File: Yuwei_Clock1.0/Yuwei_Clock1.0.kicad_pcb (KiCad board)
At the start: 2 copper layers, 140 x 90 mm, 4 parts

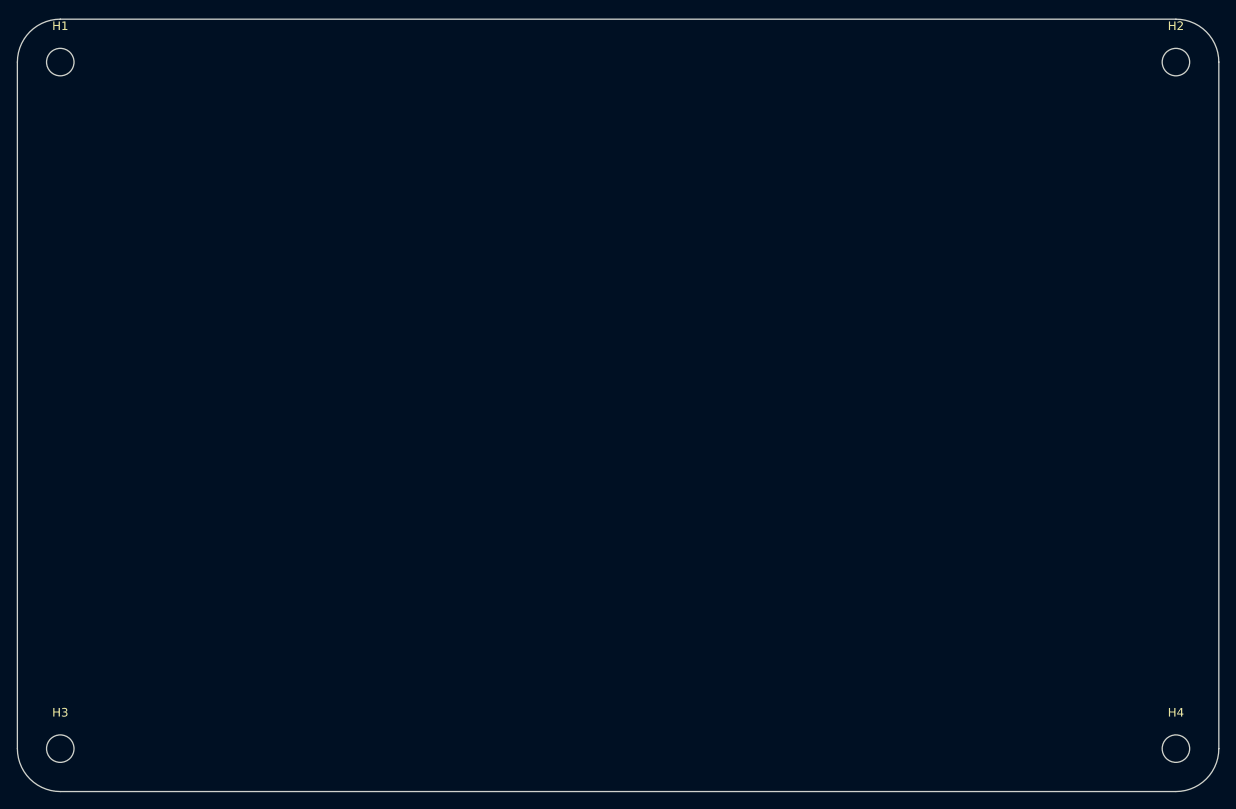
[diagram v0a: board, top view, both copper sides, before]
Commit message: Change polar capacitor to C_0805_10uf
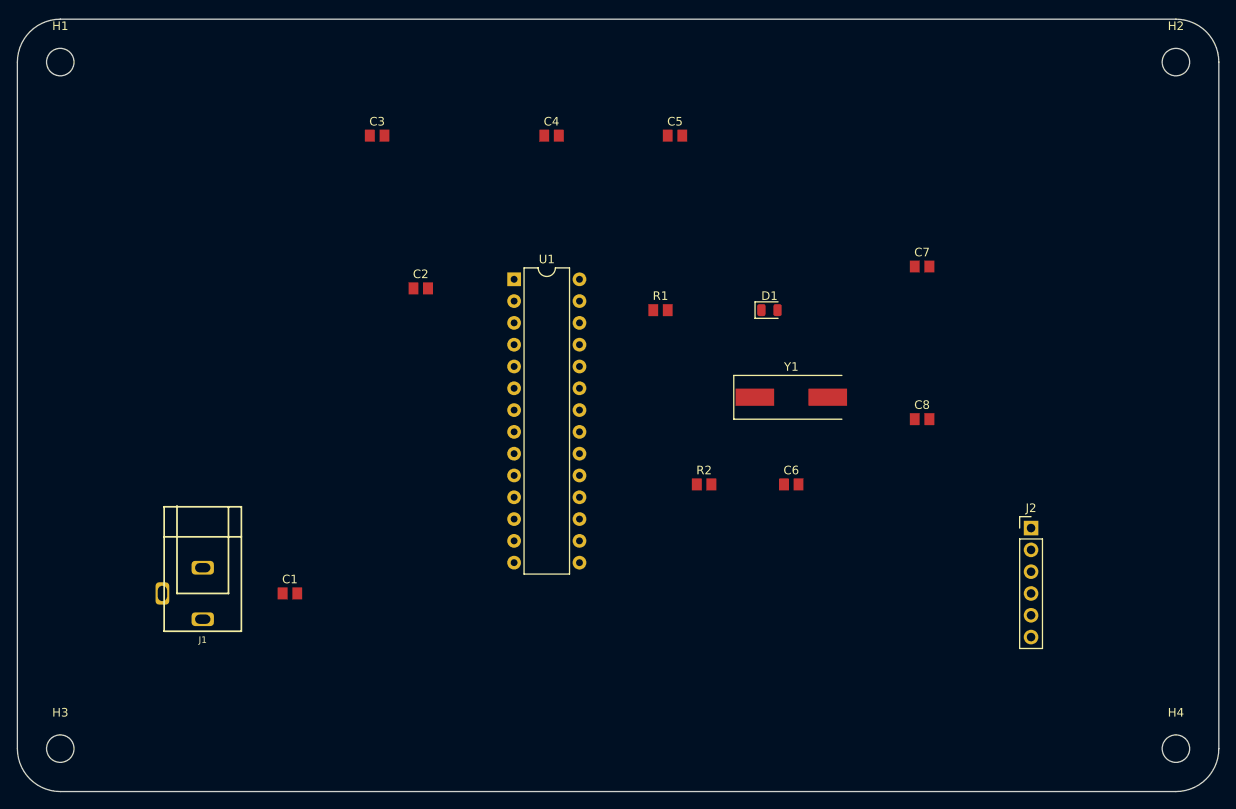
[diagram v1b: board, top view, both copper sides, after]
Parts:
- added C1: C_0805_10uf, footprints:C_0805_2012Metric, F.Cu at (111.8, 121.9)
- added C2: C_0805_10uf, footprints:C_0805_2012Metric, F.Cu at (127.0, 86.4)
- added C3: C_0805_10uf, footprints:C_0805_2012Metric, F.Cu at (121.9, 68.6)
- added C4: C_0805_10uf, footprints:C_0805_2012Metric, F.Cu at (142.2, 68.6)
- added C5: C_0805_10uf, footprints:C_0805_2012Metric, F.Cu at (156.6, 68.6)
- added C6: C_0805_0.1uf, footprints:C_0805_2012Metric, F.Cu at (170.2, 109.2)
- added C7: C_0805_22pf, footprints:C_0805_2012Metric, F.Cu at (185.4, 83.8)
- added C8: C_0805_22pf, footprints:C_0805_2012Metric, F.Cu at (185.4, 101.6)
- added D1: LED_0805, footprints:LED_0805_2012Metric, F.Cu at (167.6, 88.9)
- added J1: PJ-102AH, footprints:PJ-102AH, F.Cu at (101.6, 121.9)
- added J2: Conn_01x06, footprints:PinHeader_1x06_P2.54mm_Vertical, F.Cu at (198.1, 114.3)
- added R1: R_0805_2.2K, footprints:R_0805_2012Metric, F.Cu at (154.9, 88.9)
- added R2: R_0805_10K, footprints:R_0805_2012Metric, F.Cu at (160.0, 109.2)
- added U1: ATmega328-PU, footprints:DIP-28_W7.62mm, F.Cu at (137.9, 85.3)
- added Y1: Crystal_16MHz, footprints:Crystal_SMD_HC49-SD, F.Cu at (170.2, 99.1)

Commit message: Update with Schematic and PCB
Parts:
- removed C8: C_0805_22pf, footprints:C_0805_2012Metric
- removed J1: PJ-102AH, footprints:PJ-102AH
- added J?: Conn_01x06, footprints:PinHeader_1x06_P2.54mm_Vertical, F.Cu at (152.0, 82.1)
- added R3: R_0805_47, footprints:R_0805_2012Metric, F.Cu at (156.5, 97.1)
- added R4: R_0805_47, footprints:R_0805_2012Metric, F.Cu at (172.1, 81.3)
- added SW1: Omron_B3F_SPST, footprints:SW_SPST_Omron_B3FS-100xP, F.Cu at (143.8, 112.0)
- added U2: L7805, footprints:TO-220-3_Horizontal_TabDown, F.Cu at (141.4, 100.0)
- C2, C3: value C_0805_10uf -> C_0805_0.1uf
- C4, C5: value C_0805_10uf -> C_0805_22pf
- C6: value C_0805_0.1uf -> C_0805_1uf
- C7: value C_0805_22pf -> C_0805_1uf
- J2: value Conn_01x06 -> PJ-102AH; footprint footprints:PinHeader_1x06_P2.54mm_Vertical -> footprints:PJ-102AH
- moved C1 69.1 mm to (167.6, 81.3)
- moved C5 57.6 mm to (133.9, 121.5)
- moved C3 48.3 mm to (167.6, 84.2)
- moved D1 48.2 mm to (129.5, 118.5)
- moved J2 44.6 mm to (160.3, 90.6)
- moved R1 41.3 mm to (129.5, 121.5)
- moved C7 36.7 mm to (151.9, 98.6)
- moved C4 35.4 mm to (155.0, 101.6)
- moved C2 34.0 mm to (138.3, 118.4)
- moved R2 27.7 mm to (133.9, 118.4)
- moved Y1 25.4 mm to (145.5, 104.9)
- moved C6 25.1 mm to (172.1, 84.2)
- moved U1 9.60 mm to (128.9, 81.9)
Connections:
- C1 pad 1: Net-(C1-Pad1) -> Net-(U1-Pad21)
- C2 pad 1: Net-(C2-Pad1) -> VCC
- C3 pad 1: VCC -> RESET
- C3 pad 2: GND -> unconnected-(C3-Pad2)
- C4 pad 1: VCC -> Net-(C4-Pad1)
- C5 pad 1: VCC -> Net-(C5-Pad1)
- C6 pad 1: Net-(C6-Pad1) -> Net-(J2-Pad1)
- C6 pad 2: RTS -> GND
- C7 pad 1: /XTal1 -> VCC
- J2 pad 1: GND -> Net-(J2-Pad1)
- R2 pad 2: Net-(C6-Pad1) -> RESET
- U1 pad 1: Net-(C6-Pad1) -> RESET
- U1 pad 10: /XTal 2 -> Net-(C5-Pad1)
- U1 pad 2: Net-(J2-Pad4) -> RXD
- U1 pad 21: Net-(C2-Pad1) -> Net-(U1-Pad21)
- U1 pad 22: unconnected-(U1-Pad22) -> GND
- U1 pad 3: Net-(J2-Pad5) -> unconnected-(U1-Pad3)
- U1 pad 4: unconnected-(U1-Pad4) -> TXD
- U1 pad 9: /XTal1 -> Net-(C4-Pad1)
- Y1 pad 1: /XTal 2 -> Net-(C4-Pad1)
- Y1 pad 2: /XTal1 -> Net-(C5-Pad1)

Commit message: Update with RTC
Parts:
- added BZ1: Buzzer, footprints:Buzzer_TDK_PS1240P02BT_D12.2mm_H6.5mm, F.Cu at (134.6, 68.6)
- added DS1: LED_Display_1001, footprints:Adafruit-1001-0-0-MFG, F.Cu at (115.1, 87.5)
- added J1: Conn_01x06, footprints:PinHeader_1x06_P2.54mm_Vertical, F.Cu at (127.7, 64.0)
- added R5: R_0805_1K, footprints:R_0805_2012Metric, F.Cu at (146.2, 63.2)
- added R6: PhotoconductivePhotocell, footprints:R_LDR_4.9x4.2mm_P2.54mm_Vertical, F.Cu at (106.1, 116.2)
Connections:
- C3 pad 2: unconnected-(C3-Pad2) -> Net-(C3-Pad2)
- R3 pad 2: unconnected-(R3-Pad2) -> Net-(R3-Pad2)
- R4 pad 1: unconnected-(R4-Pad1) -> Net-(R4-Pad1)
- U1 pad 14: unconnected-(U1-Pad14) -> Net-(U1-Pad14)
- U1 pad 17: unconnected-(U1-Pad17) -> LED_SCK
- U1 pad 24: unconnected-(U1-Pad24) -> Net-(U1-Pad24)
